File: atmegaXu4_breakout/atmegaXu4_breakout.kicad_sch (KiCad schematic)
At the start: 28 parts, among them J1 USB_C_Receptacle_USB2.0, J2 Header-West, J3 Header-East, J4 AVR-ISP-6, U1 ATmega32U4-MU, U2 AP2127K-3.3

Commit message: Final DRC before release
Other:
- title: atmegaXu4_breakout -> atmega32u4_breakout
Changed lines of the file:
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@@
   (paper "A4")
   (title_block
-    (title "atmegaXu4_breakout")
+    (title "atmega32u4_breakout")
     (date "2022-12-22")
     (rev "rev B")

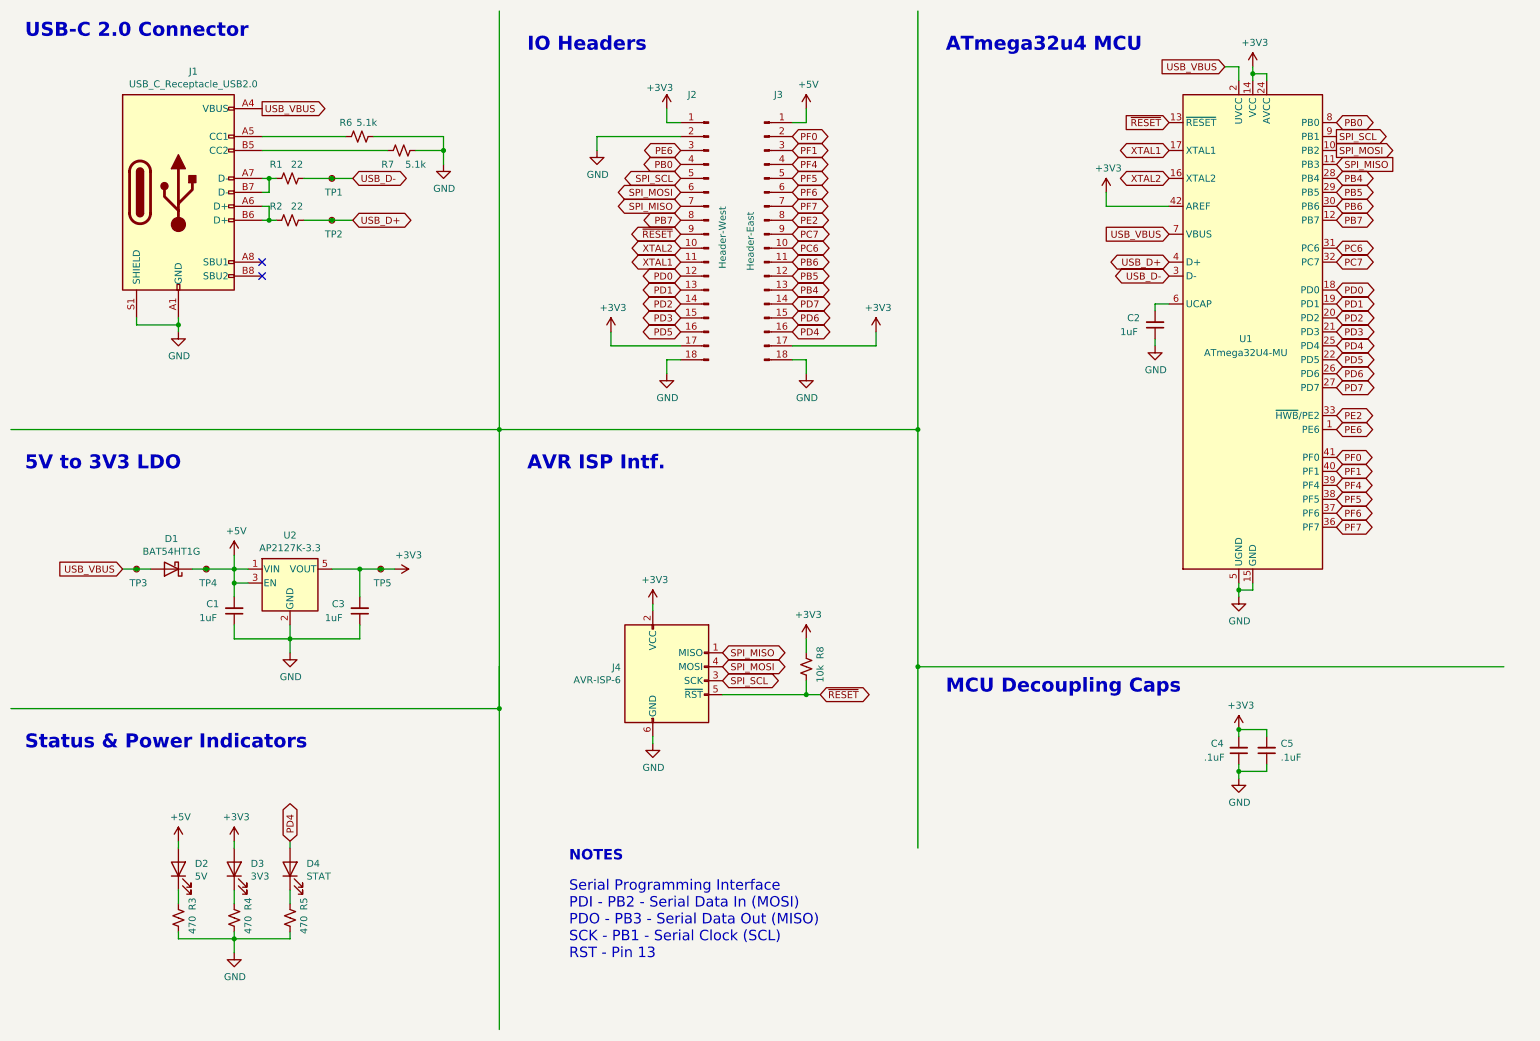
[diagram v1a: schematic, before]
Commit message: Added on-board 16MHz crystal
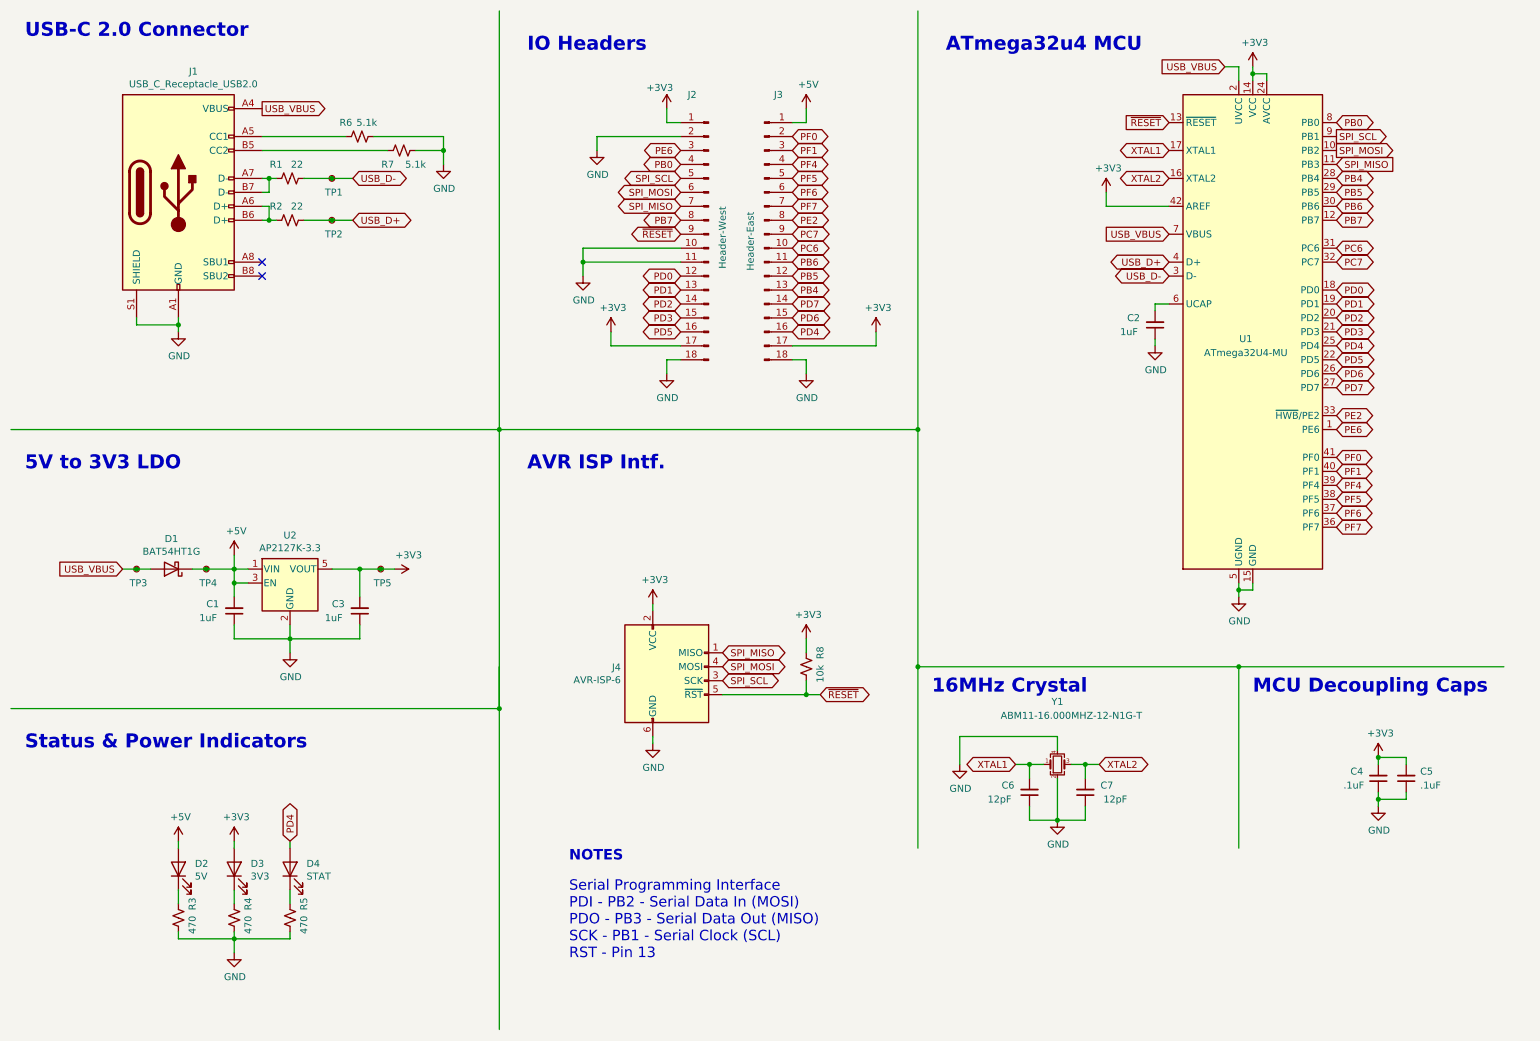
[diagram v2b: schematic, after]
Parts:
- added C6, C7: 12pF, Capacitor_SMD:C_0402_1005Metric, symbol Device:C_Small
- added Y1: ABM11-16.000MHZ-12-N1G-T, Crystal:Crystal_SMD_2016-4Pin_2.0x1.6mm, symbol Device:Crystal_GND24_Small
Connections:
- net GND: now also J2.10 (Pin_10), J2.11 (Pin_11), C6.1, C7.1, Y1.2, Y1.4
- net XTAL1: now also C6.2, Y1.1; no longer J2.11 (Pin_11)
- net XTAL2: now also C7.2, Y1.3; no longer J2.10 (Pin_10)
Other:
- note added: "16MHz Crystal"
- moved on the sheet: C4, C5
